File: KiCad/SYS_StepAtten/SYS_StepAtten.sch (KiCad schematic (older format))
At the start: 154 parts

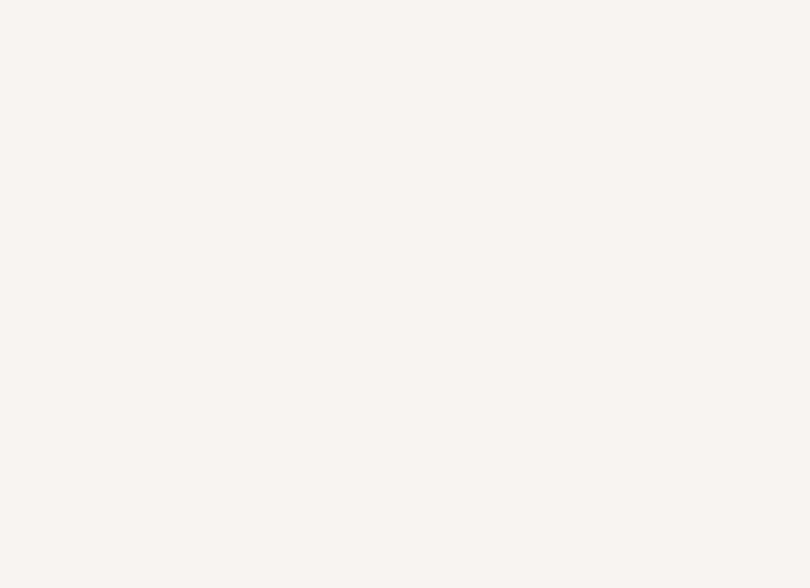
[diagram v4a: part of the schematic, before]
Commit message: Added Pulldowns on transitors
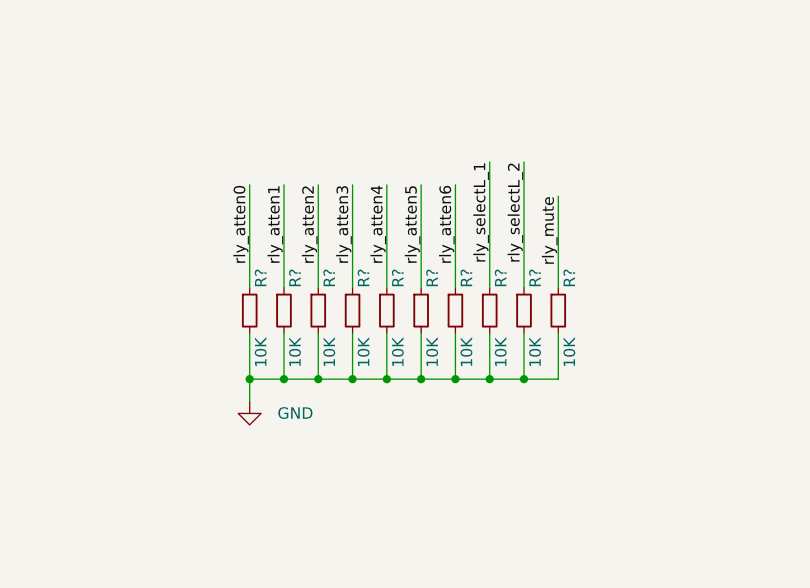
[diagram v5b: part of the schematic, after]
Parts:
- added R? (x10): 10K, symbol Device:R_Small
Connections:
- net GND: now also R?.2, R?.2, R?.2, R?.2, R?.2, R?.2, R?.2, R?.2, R?.2, R?.2
- net rly_atten0: now also R?.1
- net rly_atten1: now also R?.1
- net rly_atten2: now also R?.1
- net rly_atten3: now also R?.1
- net rly_atten4: now also R?.1
- net rly_atten5: now also R?.1
- net rly_atten6: now also R?.1
- net rly_mute: now also R?.1
- net rly_selectL_1: now also R?.1
- net rly_selectL_2: now also R?.1
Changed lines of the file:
@@
 Wire Wire Line
 	13950 2750 13950 3200
+Text Label 13400 7400 3    50   ~ 0
+rly_atten6
+Text Label 13250 7400 3    50   ~ 0
+rly_atten5
+Text Label 13100 7400 3    50   ~ 0
+rly_atten4
+Text Label 12950 7400 3    50   ~ 0
+rly_atten3
+Text Label 12800 7400 3    50   ~ 0
+rly_atten2
+Text Label 12650 7400 3    50   ~ 0
+rly_atten1
+Text Label 12500 7400 3    50   ~ 0
+rly_atten0
+Text Label 13700 7300 3    50   ~ 0
+rly_selectL_2
+Text Label 13550 7300 3    50   ~ 0
+rly_selectL_1
+Wire Wire Line
+	12500 7400 12500 7850
+Wire Wire Line
+	12650 7850 12650 7400
+Wire Wire Line
+	12800 7400 12800 7850
+Wire Wire Line
+	12950 7850 12950 7400
+Wire Wire Line
+	13100 7400 13100 7850
+Wire Wire Line
+	13250 7850 13250 7400
+Wire Wire Line
+	13400 7400 13400 7850
+Wire Wire Line
+	13550 7850 13550 7300
+Wire Wire Line
+	13700 7850 13700 7300
+Text Label 13850 7450 3    50   ~ 0
+rly_mute
+Wire Wire Line
+	13850 7450 13850 7850
+$Comp
+L Device:R_Small R?
+U 1 1 61B71073
+P 12500 7950
+F 0 "R?" V 12550 8050 50  0000 L CNN
+F 1 "10K" V 12550 7700 50  0000 L CNN
+F 2 "" H 12500 7950 50  0001 C CNN
+F 3 "~" H 12500 7950 50  0001 C CNN
+	1    12500 7950
+	1    0    0    -1
+$EndComp
+$Comp
+L Device:R_Small R?
+U 1 1 61B74BF5
+P 12650 7950
+F 0 "R?" V 12700 8050 50  0000 L CNN
+F 1 "10K" V 12700 7700 50  0000 L CNN
+F 2 "" H 12650 7950 50  0001 C CNN
+F 3 "~" H 12650 7950 50  0001 C CNN
+	1    12650 7950
+	1    0    0    -1
+$EndComp
+$Comp
+L Device:R_Small R?
+U 1 1 61B74F18
+P 12800 7950
+F 0 "R?" V 12850 8050 50  0000 L CNN
+F 1 "10K" V 12850 7700 50  0000 L CNN
+F 2 "" H 12800 7950 50  0001 C CNN
+F 3 "~" H 12800 7950 50  0001 C CNN
+	1    12800 7950
+	1    0    0    -1
+$EndComp
+$Comp
+L Device:R_Small R?
+U 1 1 61B7501A
+P 12950 7950
+F 0 "R?" V 13000 8050 50  0000 L CNN
+F 1 "10K" V 13000 7700 50  0000 L CNN
+F 2 "" H 12950 7950 50  0001 C CNN
+F 3 "~" H 12950 7950 50  0001 C CNN
+	1    12950 7950
+	1    0    0    -1
+$EndComp
+$Comp
+L Device:R_Small R?
+U 1 1 61B751DE
+P 13100 7950
+F 0 "R?" V 13150 8050 50  0000 L CNN
+F 1 "10K" V 13150 7700 50  0000 L CNN
+F 2 "" H 13100 7950 50  0001 C CNN
+F 3 "~" H 13100 7950 50  0001 C CNN
+	1    13100 7950
+	1    0    0    -1
+$EndComp
+$Comp
+L Device:R_Small R?
+U 1 1 61B7533C
+P 13250 7950
+F 0 "R?" V 13300 8050 50  0000 L CNN
+F 1 "10K" V 13300 7700 50  0000 L CNN
+F 2 "" H 13250 7950 50  0001 C CNN
+F 3 "~" H 13250 7950 50  0001 C CNN
+	1    13250 7950
+	1    0    0    -1
+$EndComp
+$Comp
+L Device:R_Small R?
+U 1 1 61B75458
+P 13400 7950
+F 0 "R?" V 13450 8050 50  0000 L CNN
+F 1 "10K" V 13450 7700 50  0000 L CNN
+F 2 "" H 13400 7950 50  0001 C CNN
+F 3 "~" H 13400 7950 50  0001 C CNN
+	1    13400 7950
+	1    0    0    -1
+$EndComp
+$Comp
+L Device:R_Small R?
+U 1 1 61B756DD
+P 13550 7950
+F 0 "R?" V 13600 8050 50  0000 L CNN
+F 1 "10K" V 13600 7700 50  0000 L CNN
+F 2 "" H 13550 7950 50  0001 C CNN
+F 3 "~" H 13550 7950 50  0001 C CNN
+	1    13550 7950
+	1    0    0    -1
+$EndComp
+$Comp
+L Device:R_Small R?
+U 1 1 61B75982
+P 13700 7950
+F 0 "R?" V 13750 8050 50  0000 L CNN
+F 1 "10K" V 13750 7700 50  0000 L CNN
+F 2 "" H 13700 7950 50  0001 C CNN
+F 3 "~" H 13700 7950 50  0001 C CNN
+	1    13700 7950
+	1    0    0    -1
+$EndComp
+$Comp
+L Device:R_Small R?
+U 1 1 61B75D0A
+P 13850 7950
+F 0 "R?" V 13900 8050 50  0000 L CNN
+F 1 "10K" V 13900 7700 50  0000 L CNN
+F 2 "" H 13850 7950 50  0001 C CNN
+F 3 "~" H 13850 7950 50  0001 C CNN
+	1    13850 7950
+	1    0    0    -1
+$EndComp
+Wire Wire Line
+	12500 8050 12500 8250
+Wire Wire Line
+	12500 8250 12650 8250
+Wire Wire Line
+	13850 8250 13850 8050
+Wire Wire Line
+	13700 8050 13700 8250
+Connection ~ 13700 8250
+Wire Wire Line
+	13700 8250 13850 8250
+Wire Wire Line
+	13550 8050 13550 8250
+Connection ~ 13550 8250
+Wire Wire Line
+	13550 8250 13700 8250
+Wire Wire Line
+	13400 8050 13400 8250
+Connection ~ 13400 8250
+Wire Wire Line
+	13400 8250 13550 8250
+Wire Wire Line
+	13250 8050 13250 8250
+Connection ~ 13250 8250
+Wire Wire Line
+	13250 8250 13400 8250
+Wire Wire Line
+	13100 8050 13100 8250
+Connection ~ 13100 8250
+Wire Wire Line
+	13100 8250 13250 8250
+Wire Wire Line
+	12950 8050 12950 8250
+Connection ~ 12950 8250
+Wire Wire Line
+	12950 8250 13100 8250
+Wire Wire Line
+	12800 8050 12800 8250
+Connection ~ 12800 8250
+Wire Wire Line
+	12800 8250 12950 8250
+Wire Wire Line
+	12650 8050 12650 8250
+Connection ~ 12650 8250
+Wire Wire Line
+	12650 8250 12800 8250
+$Comp
+L power:GND #PWR?
+U 1 1 623E9604
+P 12500 8350
+F 0 "#PWR?" H 12500 8100 50  0001 C CNN
+F 1 "GND" H 12700 8300 50  0000 C CNN
+F 2 "" H 12500 8350 50  0001 C CNN
+F 3 "" H 12500 8350 50  0001 C CNN
+	1    12500 8350
+	1    0    0    -1
+$EndComp
+Wire Wire Line
+	12500 8350 12500 8250
+Connection ~ 12500 8250
 $EndSCHEMATC

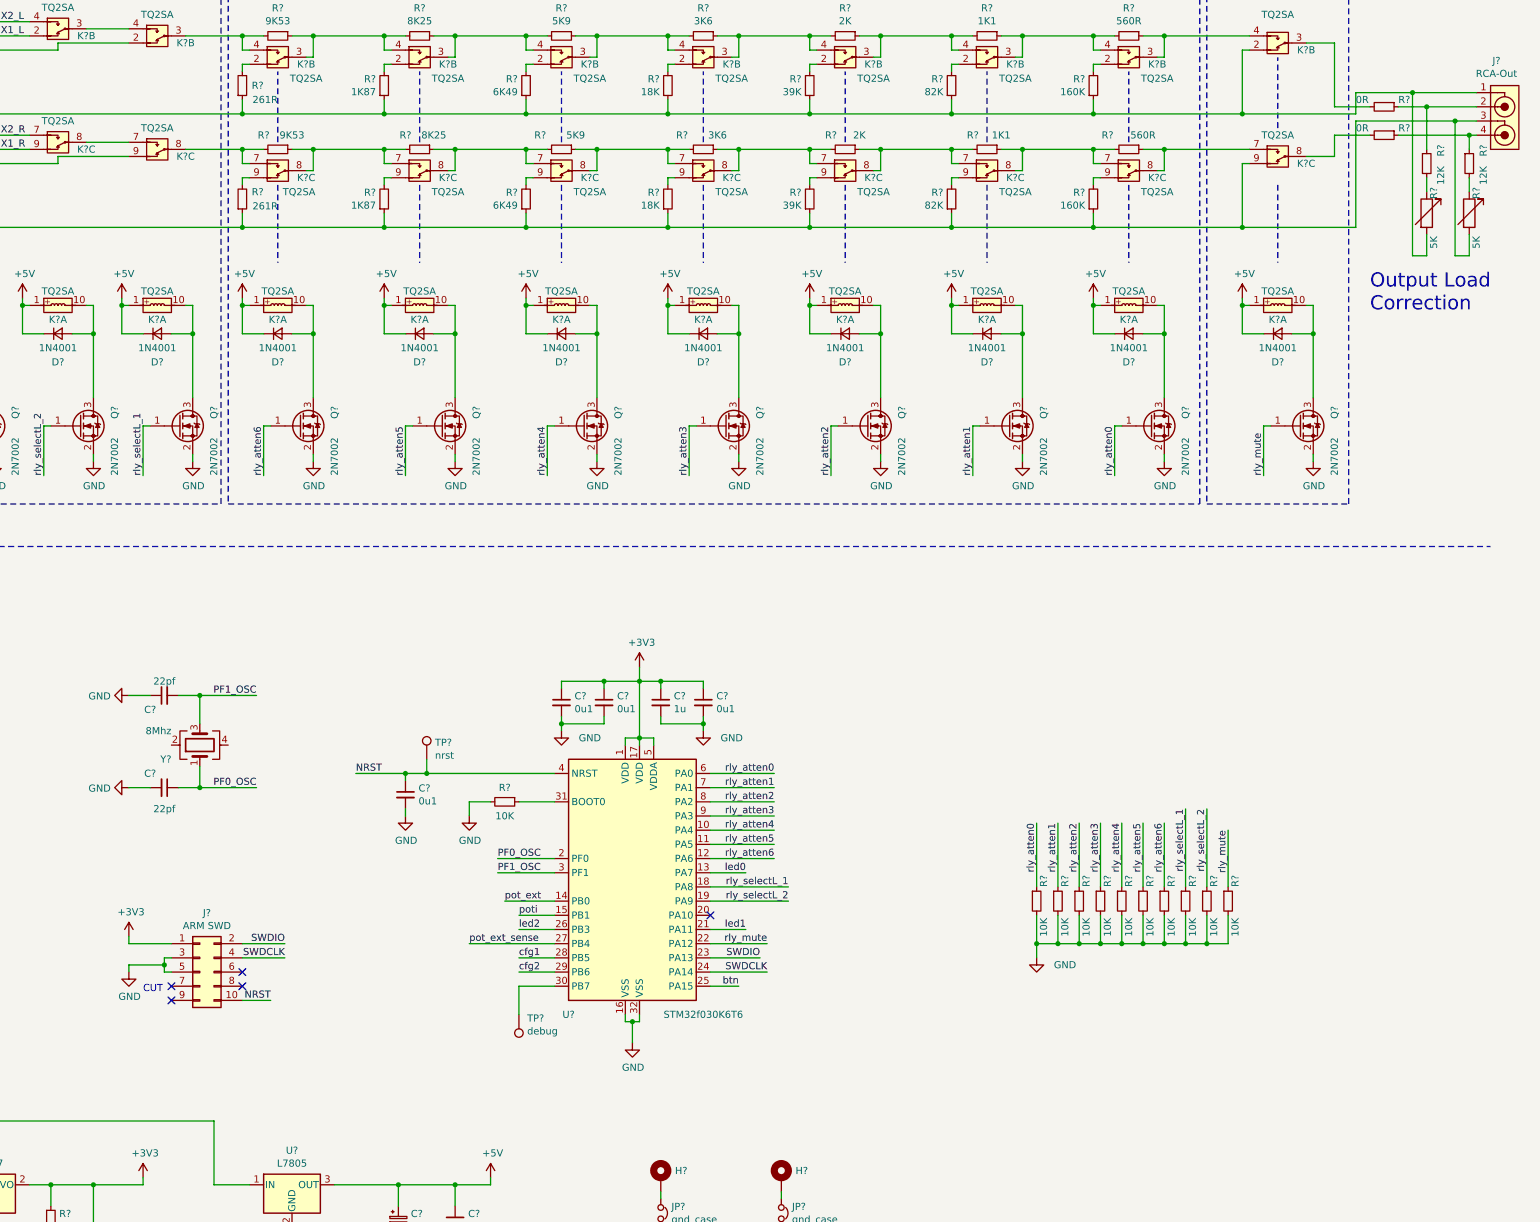
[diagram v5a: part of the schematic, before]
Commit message: Added Ground Config Jumpers
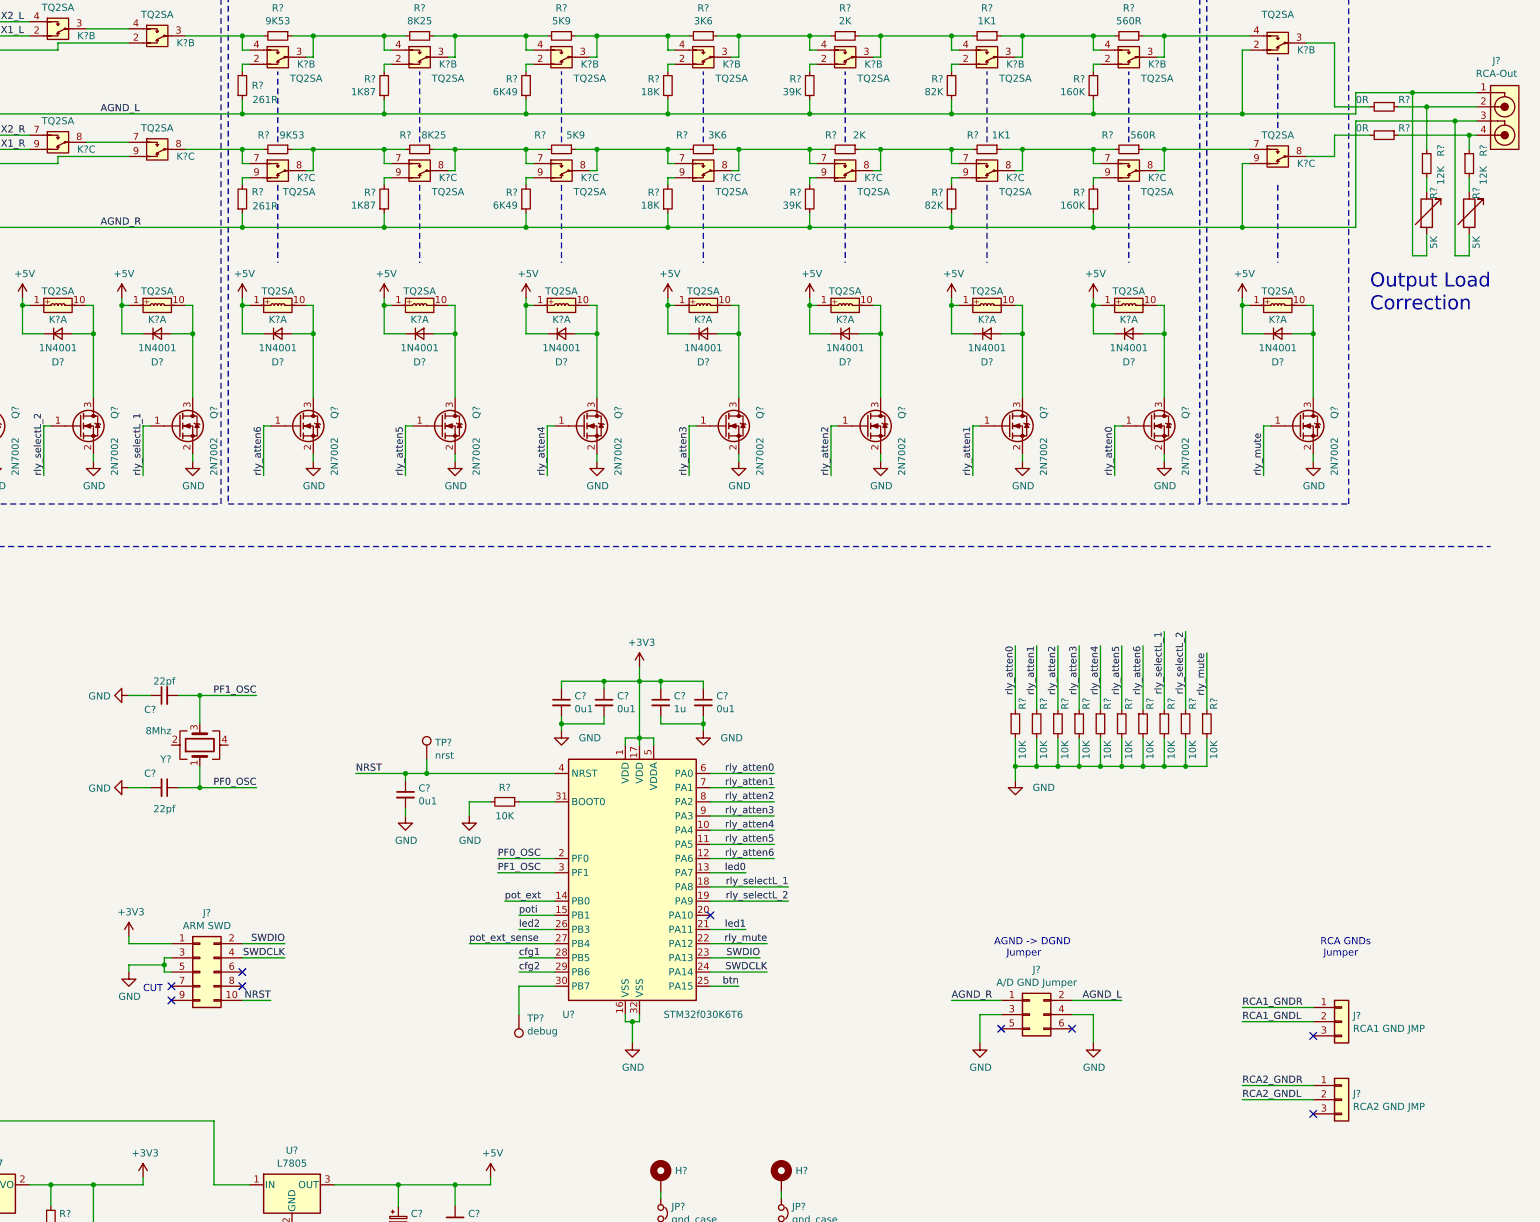
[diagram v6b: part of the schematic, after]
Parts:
- added J?: A/D GND Jumper, Connector_PinHeader_2.54mm:PinHeader_2x03_P2.54mm_Vertical, symbol Connector_Generic:Conn_02x03_Odd_Even
- added J?: RCA1 GND JMP, symbol Connector_Generic:Conn_01x03
- added J?: RCA2 GND JMP, symbol Connector_Generic:Conn_01x03
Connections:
- net GND: now also J?.3 (Pin_3), J?.4 (Pin_4)
- net RCA1_GNDL: now also J?.2 (Pin_2)
- net RCA1_GNDR: now also J?.1 (Pin_1)
- net RCA2_GNDL: now also J?.2 (Pin_2)
- net RCA2_GNDR: now also J?.1 (Pin_1)
- net AGND_L: now reaches J?.1, K?.2, K?.3, R?.1, R?.1, R?.1, R?.1, R?.1, R?.1, R?.1, R?.2
- net AGND_L: now also J?.2 (Pin_2)
- net AGND_R: now reaches J?.3, K?.8, K?.9, R?.1, R?.1, R?.1, R?.1, R?.1, R?.1, R?.1, R?.2
- net AGND_R: now also J?.1 (Pin_1)
- no-connect marks 8 -> 12
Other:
- note added: "AGND -> DGND\n Jumper\n"
- note added: "RCA GNDs \n Jumper\n"
- moved on the sheet: R?

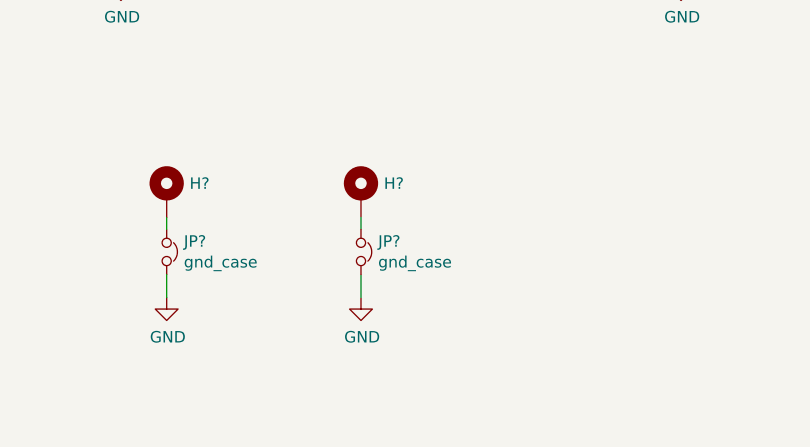
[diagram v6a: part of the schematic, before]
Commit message: Changed Mounting Hole Grounding
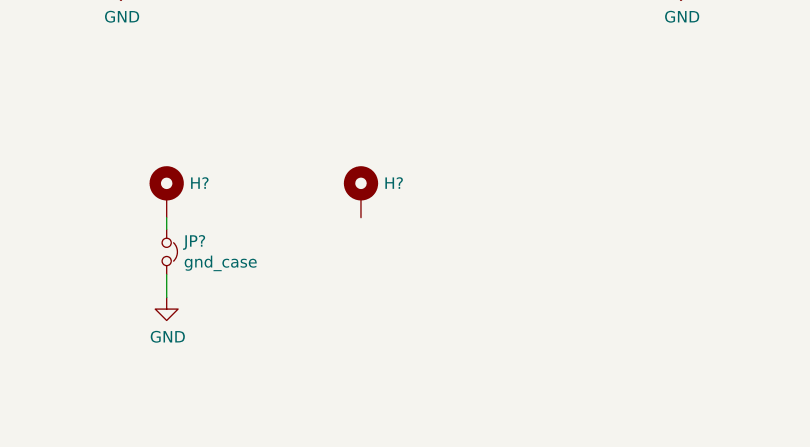
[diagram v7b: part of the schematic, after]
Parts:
- removed JP?: gnd_case, Resistor_SMD:R_0603_1608Metric, symbol Device:Jumper_NC_Small
- H? (x2): footprint MountingHole:MountingHole_3.2mm_M3_Pad_Via -> (none)
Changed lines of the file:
@@
 F 0 "H?" H 10800 9949 50  0000 L CNN
 F 1 "MountingHole 1" H 10800 9858 50  0001 L CNN
-F 2 "MountingHole:MountingHole_3.2mm_M3_Pad_Via" H 10700 9900 50  0001 C CNN
+F 2 "" H 10700 9900 50  0001 C CNN
 F 3 "~" H 10700 9900 50  0001 C CNN
 	1    10700 9900
@@
 	9150 6750 9150 6700
 Connection ~ 9150 6700
-$Comp
-L power:GND #PWR?
-U 1 1 62E79D46
-P 10700 10350
-F 0 "#PWR?" H 10700 10100 50  0001 C CNN
-F 1 "GND" H 10705 10177 50  0000 C CNN
-F 2 "" H 10700 10350 50  0001 C CNN
-F 3 "" H 10700 10350 50  0001 C CNN
-	1    10700 10350
-	1    0    0    -1
-$EndComp
-Wire Wire Line
-	10700 10350 10700 10250
 Wire Wire Line
 	4800 7000 4700 7000
@@
 F 0 "H?" H 9950 9949 50  0000 L CNN
 F 1 "MH 1" H 9950 9858 50  0001 L CNN
-F 2 "MountingHole:MountingHole_3.2mm_M3_Pad_Via" H 9850 9900 50  0001 C CNN
+F 2 "" H 9850 9900 50  0001 C CNN
 F 3 "~" H 9850 9900 50  0001 C CNN
 	1    9850 9900
@@
 	0    1    1    0
 $EndComp
-$Comp
-L Device:Jumper_NC_Small JP?
-U 1 1 5F07A360
-P 10700 10150
-F 0 "JP?" V 10654 10225 50  0000 L CNN
-F 1 "gnd_case" V 10745 10225 50  0000 L CNN
-F 2 "Resistor_SMD:R_0603_1608Metric" H 10700 10150 50  0001 C CNN
-F 3 "~" H 10700 10150 50  0001 C CNN
-	1    10700 10150
-	0    1    1    0
-$EndComp
 Wire Wire Line
 	9850 10000 9850 10050
-Wire Wire Line
-	10700 10000 10700 10050
 $Comp
 L Panasonic_TQ2SA:TQ2SA-Multi K?

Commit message: Updated Power Supply
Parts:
- added C?: 1uf, Capacitor_SMD:C_0603_1608Metric, symbol Device:C_Small
- added C?: 100u, Capacitor_SMD:CP_Elec_8x6.9, symbol Device:CP_Small
- added F?: 1A, Fuse:Fuse_1206_3216Metric, symbol Device:Polyfuse_Small
- added HS? (x2): Heatsink, XSD-C4649_TO220_Heatsink:XSD-C4649_TO220_Heatsink, symbol Mechanical:Heatsink
- added U?: L7805, Package_TO_SOT_THT:TO-220-3_Vertical, symbol Regulator_Linear:L7805
- U?: footprint Package_TO_SOT_SMD:TO-252-2 -> Package_TO_SOT_THT:TO-220-3_Vertical
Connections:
- net GND: now also C?.2, C?.2, U?.2 (GND)
- net at D?.1 (K), D?.2 (A): now also F?.1; no longer SW?.2 (B)
- net at C?.1, C?.1, D?.1 (K)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: now also U?.1 (IN)
- net +5V renamed +5V_A
- net +5V_A: no longer D?.1 (K), D?.1 (K), D?.1 (K), D?.1 (K), D?.1 (K), D?.1 (K), D?.1 (K), K?.1, K?.1, K?.1, K?.1, K?.1, K?.1, K?.1
- new net: F?.2, SW?.2 (B)
- new net +5V_B: C?.1, C?.1, D?.1 (K), D?.1 (K), D?.1 (K), D?.1 (K), D?.1 (K), D?.1 (K), D?.1 (K), K?.1, K?.1, K?.1, K?.1, K?.1, K?.1, K?.1, U?.3 (OUT)
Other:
- moved on the sheet: C?, U?
